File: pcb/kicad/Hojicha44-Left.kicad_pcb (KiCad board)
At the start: 2 copper layers, 150.5 x 114.6 mm, 54 parts

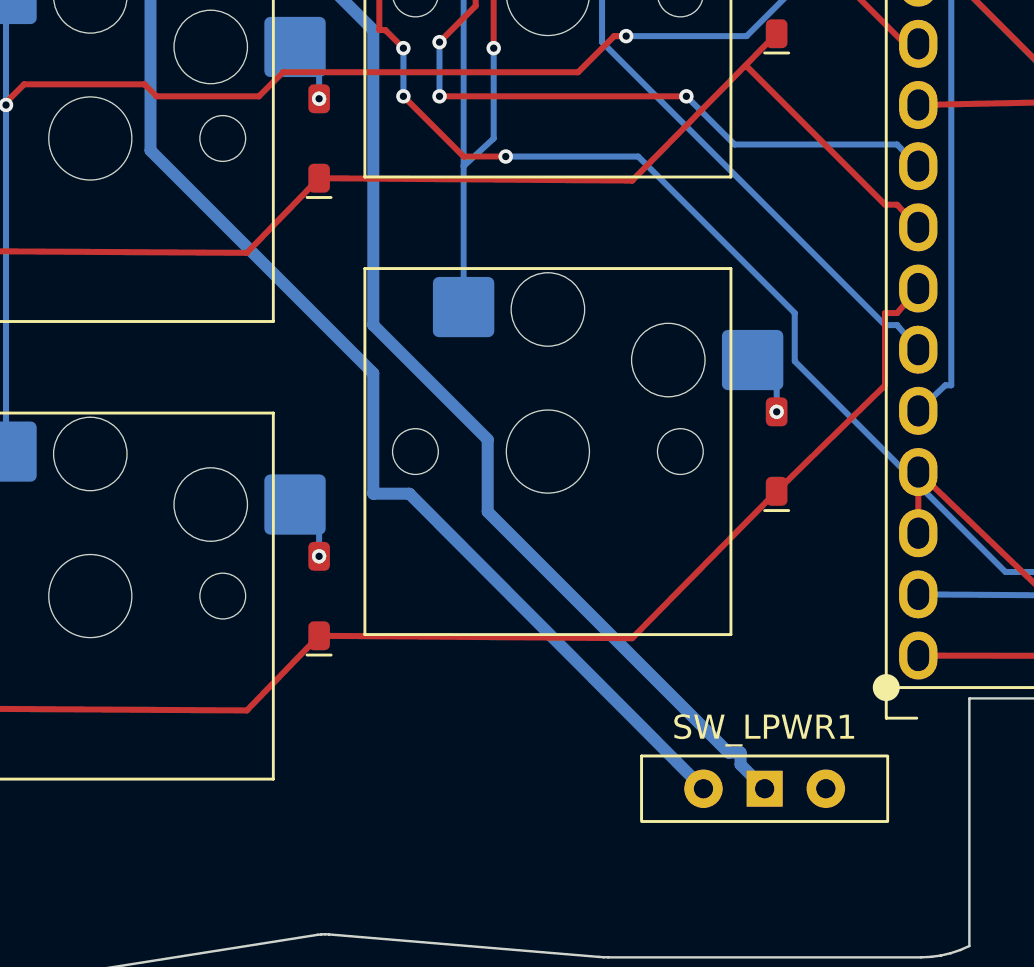
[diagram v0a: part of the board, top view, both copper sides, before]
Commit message: Review round 2: B1 pillar clearance blocker + T4 cover magnets + M2 pwrsw shift + M1 floor ruler + gate hardening
B1 (blocker): tab pillar fuse reached 1.0mm inboard of the rim - solid
case material under the PCB at all 8 stations (board rests ~1.05mm
high, bottom pads unload). Pillar now starts 0.3 outboard of the rim;
new gates: per-tab footprint-clear probes + plan-wide PCB-rim sweep
at z=-1.0. First attempt (fuse deletion) was wrong - the gates caught
it: the tab lobes are cavity in the v3.1 dilation, the fuse IS the
shelf. Tub 68.0 -> 67.4 cm3.

T4: cover magnets 04x1.5 (16 pcs, pocket 1.7, floor 0.8 -> 1.3mm);
faces still meet at the lip plane; BOM rows added (magnets were
missing entirely); first-article pull test >=1.5 kg.

M2: pwrsw footprint 2mm west (ergogen [9,14]->[7,14]) so the blade
band sits under the SAT-constrained mouth window. Left stub endpoints
moved; Right's 31 stale hand-routed pwrsw items deleted (router
re-routes fresh). Router: obstacle model seeded with preserved GUI
copper at exact clearance (MARGIN-inflated seed rejected the legal
COL5_R corridor); copper checker sees merged board with dangle
reporting scoped to preserved items; co-located router/GUI vias
deduped. DRC both halves clean (W1 set only).

M1: floor derivation rewritten to the measured below-PCB ruler
(encoder legs -3.65 from the vendored STEP - deepest; sockets are
top-side and never provisioned the floor). FLOOR_Z -5.6 keeps
~1.95mm - no geometry change.

M6/M7/M8: gen_cover in CI; stack-ties in spec_checks.cjs; pwrsw in
plate tab eligibility (DXFs byte-identical); definitive encoder web
print (cutouts 9.15 / windows 3.65 / ports 4.92-5.35).

H1: Choc 15.0 kept with honest wording (lower body 13.8, clips never
engage at 15.0/1.5mm - coherent with the plate; rev-2 coupon decides).
LOW doc cluster: TRRS chord 6.42-at-lip, encoder 24.04 shaft-center
rationale, HISTORICAL annotations on pre-fix rows, DXF layer docstring
PORON, v3.4 changelog axis 2.4->2.5 noted.
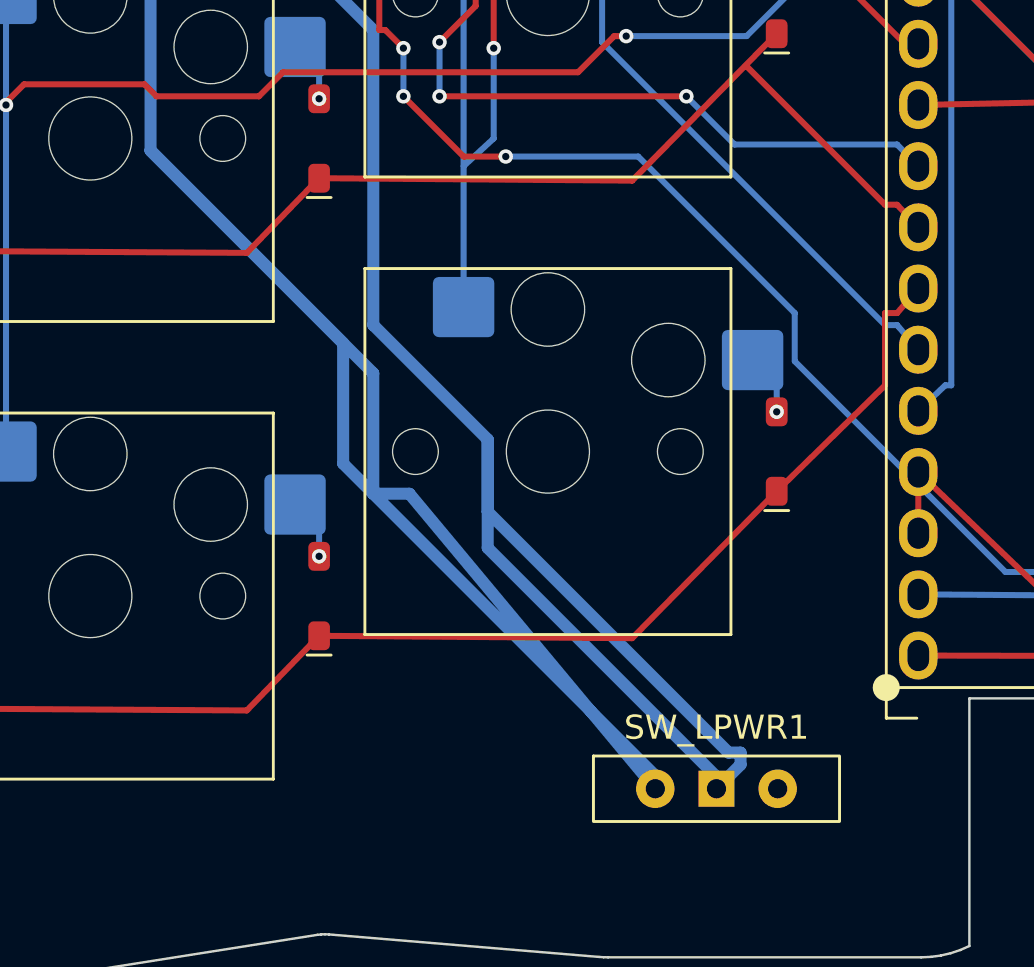
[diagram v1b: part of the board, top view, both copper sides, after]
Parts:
- moved SW_LPWR1 2.00 mm to (102.0, 51.0)
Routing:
- net /VBAT_SW_L: track 184.8 -> 218.7 mm
- net Net-(J_L2-Pin_1): track 129.7 -> 148.1 mm
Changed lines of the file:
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@@
 	(generator_version "10.0")
 	(layer "F.Cu")
-	(at 104.0 51.0 0)
+	(at 102.0 51.0 0)
 	(descr "Wuerth, WS-SLTV, 450301014042, https://www.we-online.com/components/products/datasheet/450301014042.pdf")
 	(tags "switch single-pole opposite-side-connection double-throw SPDT würth wurth")
@@
 	(segment (start 87.75 19.5) (end 87.75 31.75) (width 0.5) (layer "B.Cu") (net 45))
 	(segment (start 87.75 31.75) (end 92.5 36.5) (width 0.5) (layer "B.Cu") (net 45))
-	(segment (start 92.5 36.5) (end 92.5 39.5) (width 0.5) (layer "B.Cu") (net 45))
-	(segment (start 92.5 39.5) (end 102.5 49.5) (width 0.5) (layer "B.Cu") (net 45))
-	(segment (start 102.5 49.5) (end 103.0 49.5) (width 0.5) (layer "B.Cu") (net 45))
-	(segment (start 103.0 49.5) (end 103.0 50.0) (width 0.5) (layer "B.Cu") (net 45))
-	(segment (start 103.0 50.0) (end 104.0 51.0) (width 0.5) (layer "B.Cu") (net 45))
-	(segment (start 101.46 51.0) (end 89.25 38.75) (width 0.5) (layer "B.Cu") (net 20))
-	(segment (start 89.25 38.75) (end 87.75 38.75) (width 0.5) (layer "B.Cu") (net 20))
-	(segment (start 87.75 38.75) (end 87.75 33.75) (width 0.5) (layer "B.Cu") (net 20))
-	(segment (start 87.75 33.75) (end 78.5 24.5) (width 0.5) (layer "B.Cu") (net 20))
+	(segment (start 92.5 36.5) (end 92.5 41.0) (width 0.5) (layer "B.Cu") (net 45))
+	(segment (start 92.5 41.0) (end 102.0 50.5) (width 0.5) (layer "B.Cu") (net 45))
+	(segment (start 102.0 50.5) (end 102.0 51.0) (width 0.5) (layer "B.Cu") (net 45))
+	(segment (start 99.46 51.0) (end 99.5 50.5) (width 0.5) (layer "B.Cu") (net 20))
+	(segment (start 99.5 50.5) (end 86.5 37.5) (width 0.5) (layer "B.Cu") (net 20))
+	(segment (start 86.5 37.5) (end 86.5 32.5) (width 0.5) (layer "B.Cu") (net 20))
+	(segment (start 86.5 32.5) (end 78.5 24.5) (width 0.5) (layer "B.Cu") (net 20))
 	(segment (start 78.5 24.5) (end 78.5 12.5) (width 0.5) (layer "B.Cu") (net 20))
 	(segment (start 78.5 12.5) (end 73.75 7.75) (width 0.5) (layer "B.Cu") (net 20))
@@
 	(via (at 110.5 -13.5) (size 0.6) (drill 0.3) (layers "F.Cu" "B.Cu") (net 22))
 	(via (at 129.75 -19.75) (size 0.6) (drill 0.3) (layers "F.Cu" "B.Cu") (net 22))
+(segment (start 92.5 36.5) (end 92.5 39.5) (width 0.5) (layer "B.Cu") (net 45))
+(segment (start 92.5 39.5) (end 102.5 49.5) (width 0.5) (layer "B.Cu") (net 45))
+(segment (start 102.5 49.5) (end 103.0 49.5) (width 0.5) (layer "B.Cu") (net 45))
+(segment (start 103.0 49.5) (end 103.0 50.0) (width 0.5) (layer "B.Cu") (net 45))
+(segment (start 103.0 50.0) (end 102.0 51.0) (width 0.5) (layer "B.Cu") (net 45))
+(segment (start 99.46 51.0) (end 89.25 38.75) (width 0.5) (layer "B.Cu") (net 20))
+(segment (start 89.25 38.75) (end 87.75 38.75) (width 0.5) (layer "B.Cu") (net 20))
+(segment (start 87.75 38.75) (end 87.75 33.75) (width 0.5) (layer "B.Cu") (net 20))
+(segment (start 87.75 33.75) (end 78.5 24.5) (width 0.5) (layer "B.Cu") (net 20))
 )

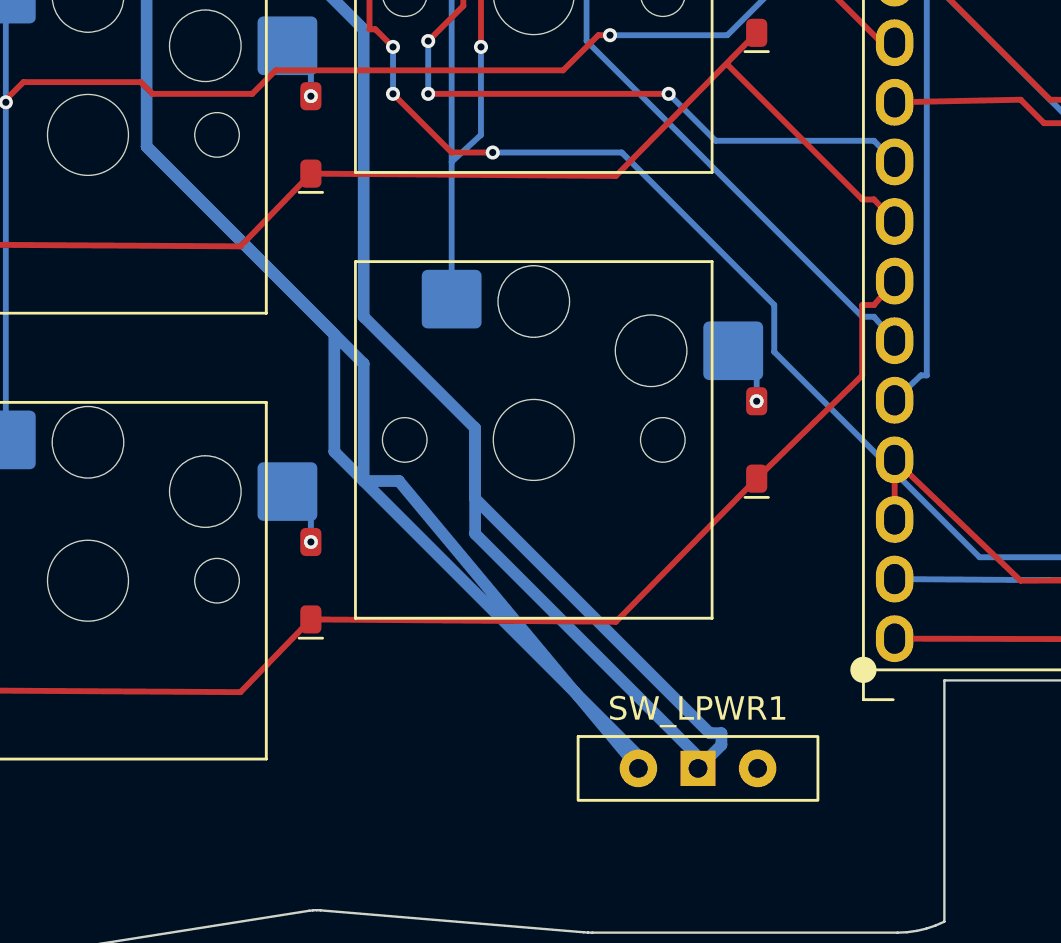
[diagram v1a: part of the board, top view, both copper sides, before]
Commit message: M3: recentre pwrsw to SAT window centres 106.3/185.2 — plateau frozen to committed Edge.Cuts, routes regenerated (nets 20/45 router-owned, silk ref_shift mirrored)
Multi-model datasheet verification overturned the M2 offset reading; the
switch is now centred on the SAT-pinned window on both halves (mirror-exact
about x=145.75). Window tracks the switch via ergogen pwrsw shift 11.3;
plateau decoupled and frozen so frame stays axis-exact. Gates: gen_pcb exit
0, DRC 28 x W1-waived per half only, ERC 0 err / 5 spare warns per half,
topology 0 dangling, npm test green, plate --check CLEAN, case+cover
regenerated with census green. Switch body 101.3..111.3, lever band
0.70/side vs window - was 4.3 mm outboard with zero visible blade.
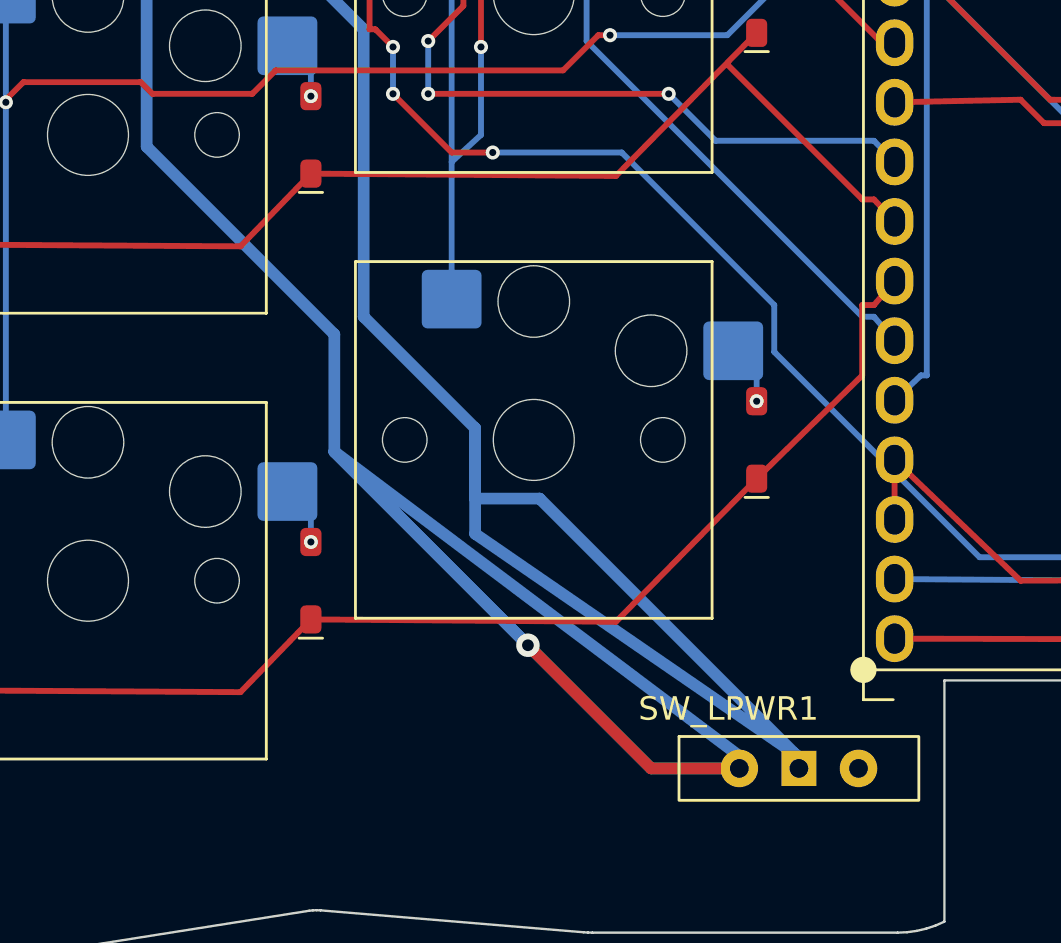
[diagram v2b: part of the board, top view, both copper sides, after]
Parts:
- moved SW_LPWR1 4.30 mm to (106.3, 51.0)
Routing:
- net /VBAT_SW_L: track 218.7 -> 232.1 mm, vias 3 -> 4
- net Net-(J_L2-Pin_1): track 148.1 -> 153.7 mm
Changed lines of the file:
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@@
 	(generator_version "10.0")
 	(layer "F.Cu")
-	(at 102.0 51.0 0)
+	(at 106.3 51.0 0)
 	(descr "Wuerth, WS-SLTV, 450301014042, https://www.we-online.com/components/products/datasheet/450301014042.pdf")
 	(tags "switch single-pole opposite-side-connection double-throw SPDT würth wurth")
 	(property "Reference" "SW_LPWR1"
-		(at 0 -2.54 0)
+		(at -3.0 -2.54 0)
 		(layer "F.SilkS")
 		(effects
@@
 	(segment (start 87.75 19.5) (end 87.75 31.75) (width 0.5) (layer "B.Cu") (net 45))
 	(segment (start 87.75 31.75) (end 92.5 36.5) (width 0.5) (layer "B.Cu") (net 45))
-	(segment (start 92.5 36.5) (end 92.5 41.0) (width 0.5) (layer "B.Cu") (net 45))
-	(segment (start 92.5 41.0) (end 102.0 50.5) (width 0.5) (layer "B.Cu") (net 45))
-	(segment (start 102.0 50.5) (end 102.0 51.0) (width 0.5) (layer "B.Cu") (net 45))
-	(segment (start 99.46 51.0) (end 99.5 50.5) (width 0.5) (layer "B.Cu") (net 20))
-	(segment (start 99.5 50.5) (end 86.5 37.5) (width 0.5) (layer "B.Cu") (net 20))
+	(segment (start 92.5 36.5) (end 92.5 39.5) (width 0.5) (layer "B.Cu") (net 45))
+	(segment (start 92.5 39.5) (end 95.25 39.5) (width 0.5) (layer "B.Cu") (net 45))
+	(segment (start 95.25 39.5) (end 106.25 50.5) (width 0.5) (layer "B.Cu") (net 45))
+	(segment (start 106.25 50.5) (end 106.3 51.0) (width 0.5) (layer "B.Cu") (net 45))
+	(segment (start 103.76 51.0) (end 100.0 51.0) (width 0.5) (layer "B.Cu") (net 20))
+	(segment (start 100.0 51.0) (end 86.5 37.5) (width 0.5) (layer "B.Cu") (net 20))
 	(segment (start 86.5 37.5) (end 86.5 32.5) (width 0.5) (layer "B.Cu") (net 20))
 	(segment (start 86.5 32.5) (end 78.5 24.5) (width 0.5) (layer "B.Cu") (net 20))
@@
 	(via (at 110.5 -13.5) (size 0.6) (drill 0.3) (layers "F.Cu" "B.Cu") (net 22))
 	(via (at 129.75 -19.75) (size 0.6) (drill 0.3) (layers "F.Cu" "B.Cu") (net 22))
-(segment (start 92.5 36.5) (end 92.5 39.5) (width 0.5) (layer "B.Cu") (net 45))
-(segment (start 92.5 39.5) (end 102.5 49.5) (width 0.5) (layer "B.Cu") (net 45))
-(segment (start 102.5 49.5) (end 103.0 49.5) (width 0.5) (layer "B.Cu") (net 45))
-(segment (start 103.0 49.5) (end 103.0 50.0) (width 0.5) (layer "B.Cu") (net 45))
-(segment (start 103.0 50.0) (end 102.0 51.0) (width 0.5) (layer "B.Cu") (net 45))
-(segment (start 99.46 51.0) (end 89.25 38.75) (width 0.5) (layer "B.Cu") (net 20))
-(segment (start 89.25 38.75) (end 87.75 38.75) (width 0.5) (layer "B.Cu") (net 20))
-(segment (start 87.75 38.75) (end 87.75 33.75) (width 0.5) (layer "B.Cu") (net 20))
-(segment (start 87.75 33.75) (end 78.5 24.5) (width 0.5) (layer "B.Cu") (net 20))
+(segment (start 103.76 51.0) (end 100.0 51.0) (width 0.5) (layer "F.Cu") (net 20))
+(segment (start 100.0 51.0) (end 94.75 45.75) (width 0.5) (layer "F.Cu") (net 20))
+(segment (start 94.75 45.75) (end 86.5 37.5) (width 0.5) (layer "B.Cu") (net 20))
+(via (at 94.75 45.75) (size 1.0) (drill 0.5) (layers "F.Cu" "B.Cu") (net 20))
+(segment (start 92.5 36.5) (end 92.5 41.0) (width 0.5) (layer "B.Cu") (net 45))
+(segment (start 92.5 41.0) (end 106.3 50.5) (width 0.5) (layer "B.Cu") (net 45))
+(segment (start 106.3 50.5) (end 106.3 51.0) (width 0.5) (layer "B.Cu") (net 45))
+(segment (start 103.76 51.0) (end 103.8 50.5) (width 0.5) (layer "B.Cu") (net 20))
+(segment (start 103.8 50.5) (end 86.5 37.5) (width 0.5) (layer "B.Cu") (net 20))
 )

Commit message: M3.1: post-audit P0 batch + provenance pipeline
- gen_pcb: pcb/kicad/hand-copper.txt manifest replaces the
  classify-by-reproduction heuristic (phase-1 deleted; extraction reads
  the committed baseline via git HEAD; copper gates before write; a
  DRC-rejected board is archived + reverted so it never feeds the next
  build). Idempotency proven: three consecutive regens byte-identical
  modulo uuid/date, DRC clean (28 W1-waived only); Left corridor
  regenerated fresh and converged (the 6 stale corridor items were
  router-owned; frozen they pinned a 1.0607mm via collision).
- gen_route: via rules from this round stand — signal pads 0.60->0.65
  (annular), same-net pairs keep the drill rule, cross-net pairs use
  the pad rule, later nets yield to earlier vias; ROUTER_VERSION r13.
- gen_schematic: POWER netclass patterns; ERC 0 errors.
- plate: USB-plug bay floor scan re-anchored on the config usb mouth
  (band-min grabbed the west-edge outline); all plate gates CLEAN.
- case: P0 magnet policy (pocket 4.3, web 1.15, band 6.6) now backed
  by CASE_OUTSET 7.0->7.1 — physical band 6.5->6.6 exactly; stations
  6/7, wall_min 1.60; cover reuses the tub scan (web 1.15).
- keymap: right thumbs RSFT/RALT/mo2/ENTER, right inner BSLH/RBKT/ESC,
  3rd layer raise_layer; spec_checks derives the 46-position list from
  layout.yaml; layout.yaml open_points drops the resolved chord item.
- make_release: dirty-tree refusal + ERC/DRC report gating + ENIG
  stamp; checks.yml board_gates job; doc sweeps (README, case/README,
  spec/case.md, notes.md 2026-10-19 section).
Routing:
- net /COL3_L: vias 2 -> 3
